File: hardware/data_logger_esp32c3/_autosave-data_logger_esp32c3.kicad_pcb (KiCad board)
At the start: 2 copper layers, 39.2 x 51.4 mm, 58 parts, among them U1 ESP32-C3-MINI-1, U2 MC34063ADRJR, U3 LM321MF, U4 LM321MF, U5 LM321MF, U6 LM321MF, U7 LM321MF, U8 LM321MF

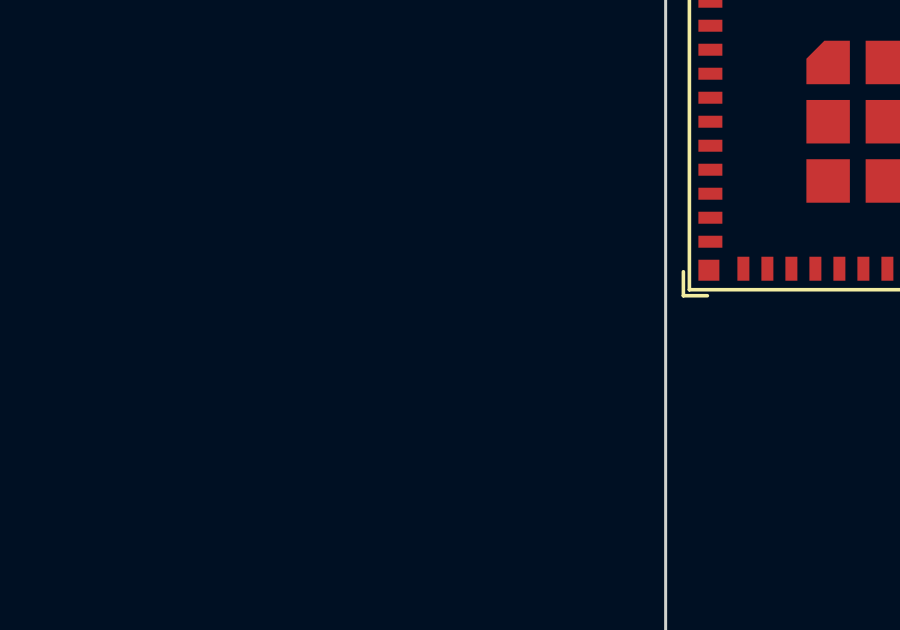
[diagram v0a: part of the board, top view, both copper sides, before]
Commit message: Added relative path libraries for kicad
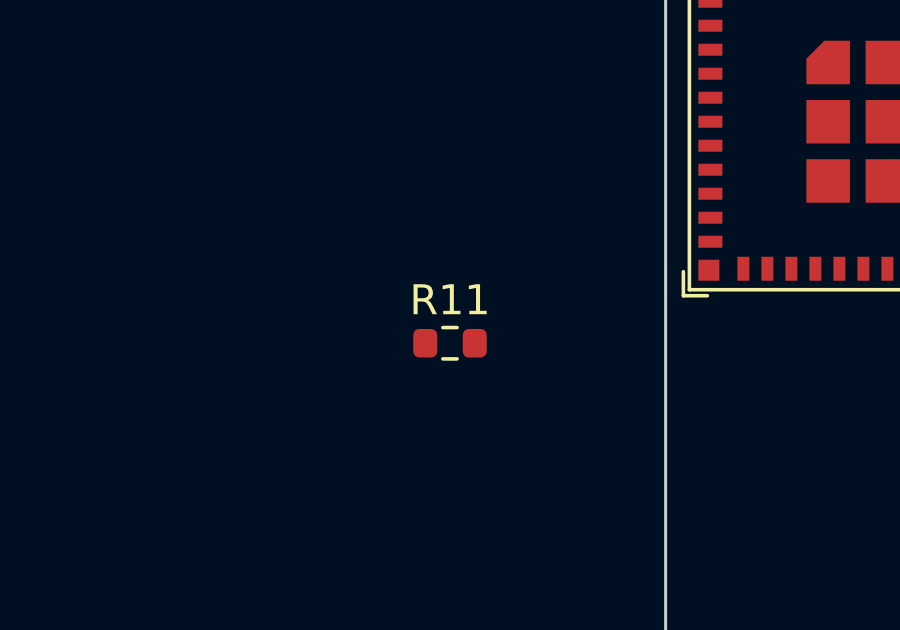
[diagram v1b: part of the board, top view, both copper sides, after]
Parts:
- added R11: 3.92k, Resistor_SMD:R_0603_1608Metric, F.Cu at (186.6, 71.4)
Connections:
- D3 pad 1: Net-(L1-Pad1) -> Net-(D3-Pad1)
- L1 pad 1: Net-(L1-Pad1) -> Net-(D3-Pad1)
- U2 pad 2: Net-(L1-Pad1) -> Net-(D3-Pad1)
